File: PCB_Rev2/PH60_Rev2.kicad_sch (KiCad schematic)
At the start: 20 parts, among them J2 Conn_01x04, J3 Conn_01x02, Q1 AO3407, Q2 AO3407, U1 E73-2G4M08S1C, U2 AP2112K-3.3, U3 TP4054, U4 ProMicro, X1 32768kHz

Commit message: Rename
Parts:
- removed D63: 1N5819, Diode_SMD:D_SOD-323F, symbol nrfmicro-rescue:MBR0520
- removed D64: BLUE, LED_SMD:LED_0603_1608Metric, symbol Device:LED
- removed D65: RED, LED_SMD:LED_0603_1608Metric, symbol Device:LED
- removed J2: Conn_01x04, Connector_FFC-FPC:Molex_200528-0040_1x04-1MP_P1.00mm_Horizontal, symbol Connector_Generic:Conn_01x04
- removed J3: Conn_01x02, Connector_Molex:Molex_PicoBlade_53261-0271_1x02-1MP_P1.25mm_Horizontal, symbol Connector_Generic:Conn_01x02
- removed JP1: SolderJumper_2_Open, nrfmicro:Jumper_SMD, symbol Jumper:SolderJumper_2_Open
- removed Q1, Q2: AO3407, Package_TO_SOT_SMD:SOT-23, symbol nrfmicro-rescue:BSS83P
- removed R1: 100K, Resistor_SMD:R_0603_1608Metric, symbol nrfmicro-rescue:R
- removed R4, R8: 1K, Resistor_SMD:R_0603_1608Metric, symbol nrfmicro-rescue:R
- removed R5: RPROG, Resistor_SMD:R_0603_1608Metric, symbol nrfmicro-rescue:R
- removed R6: 820K, Resistor_SMD:R_0603_1608Metric, symbol Device:R
- removed R7, R9: 2M, Resistor_SMD:R_0603_1608Metric, symbol Device:R
- removed U1: E73-2G4M08S1C, nrfmicro:E73-2G4M08S1C-52840, symbol nrfmicro:E73-2G4M08S1C-52840
- removed U2: AP2112K-3.3, Package_TO_SOT_SMD:SOT-23-5, symbol Regulator_Linear:AP2112K-3.3
- removed U3: TP4054, Package_TO_SOT_SMD:SOT-23-5, symbol Battery_Management:MCP73832-2-OT
- removed U4: ProMicro, nrfmicro:pro_micro, symbol nrfmicro-rescue:ProMicro
- removed X1: 32768kHz, Crystal:Crystal_SMD_3215-2Pin_3.2x1.5mm, symbol Device:Crystal_Small
- added C1, C4: 10u, Capacitor_SMD:C_0402_1005Metric, symbol Device:C
- added C10, C8: 1u, Capacitor_SMD:C_0402_1005Metric, symbol Device:C
- added C11, C12, C13, C14, C15, C16, C5, C6, C7, C9: 100n, Capacitor_SMD:C_0402_1005Metric, symbol Device:C
- added C2, C3: 15p, Capacitor_SMD:C_0402_1005Metric, symbol Device:C
- added J2: Conn_01x02, Connector_PinHeader_1.00mm:PinHeader_1x02_P1.00mm_Vertical, symbol Connector_Generic:Conn_01x02
- added J3: Conn_01x04, Connector_FFC-FPC:Molex_200528-0040_1x04-1MP_P1.00mm_Horizontal, symbol Connector_Generic:Conn_01x04
- added R1, R5: 1k, Resistor_SMD:R_0402_1005Metric, symbol Device:R
- added R2: DNF, Resistor_SMD:R_0402_1005Metric, symbol Device:R
- added R3, R4: 27.4, Resistor_SMD:R_0402_1005Metric, symbol Device:R
- added U1: NCP1117-3.3_SOT223, Package_TO_SOT_SMD:SOT-223-3_TabPin2, symbol Regulator_Linear:NCP1117-3.3_SOT223
- added U2: W25Q128JVS, Package_SO:SOIC-8_5.23x5.23mm_P1.27mm, symbol Memory_Flash:W25Q128JVS
- added U3: RP2040, Package_DFN_QFN:QFN-56-1EP_7x7mm_P0.4mm_EP3.2x3.2mm, symbol MCU_RaspberryPi:RP2040
- added Y1: Crystal_GND24, Crystal:Crystal_SMD_3225-4Pin_3.2x2.5mm, symbol Device:Crystal_GND24
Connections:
- net GND: now also C1.2, C10.2, C2.2, C3.2, C4.2, C5.2, C6.2, C7.2, C8.2, J2.2 (Pin_2), J3.4 (Pin_4), U1.1 (GND), U2.4 (GND), U3.19 (TESTEN), U3.57 (GND), Y1.2, Y1.4
- net SWD: now also U3.25 (SWD)
- net VBUS: now also C1.1, J3.1 (Pin_1), U1.3 (VI)
- net col_0: now also U3.2 (GPIO0)
- net col_1: now also U3.3 (GPIO1)
- net col_10: now also U3.13 (GPIO10)
- net col_11: now also U3.14 (GPIO11)
- net col_12: now also U3.15 (GPIO12)
- net col_13: now also U3.16 (GPIO13)
- net col_2: now also U3.4 (GPIO2)
- net col_3: now also U3.5 (GPIO3)
- net col_4: now also U3.6 (GPIO4)
- net col_5: now also U3.7 (GPIO5)
- net col_6: now also U3.8 (GPIO6)
- net col_7: now also U3.9 (GPIO7)
- net col_8: now also U3.11 (GPIO8)
- net col_9: now also U3.12 (GPIO9)
- net row_0: now also U3.17 (GPIO14)
- net row_1: now also U3.18 (GPIO15)
- net row_2: now also U3.27 (GPIO16)
- net row_3: now also U3.28 (GPIO17)
- net row_4: now also U3.29 (GPIO18)
- new net: C11.2, C12.2, C13.2, C14.2, C15.2, C16.2, C9.2
- new net: R4.2, U3.46 (USB_DM)
- new net: C3.1, R5.1, Y1.1
- new net: R3.2, U3.47 (USB_DP)
- new net +1V1: C6.1, C7.1, C8.1, U3.23 (DVDD), U3.45 (VREG_VOUT), U3.50 (DVDD)
- new net +3V3: C10.1, C11.1, C12.1, C13.1, C14.1, C15.1, C16.1, C4.1, C5.1, C9.1, R2.1, U1.2 (VO), U2.8 (VCC), U3.1 (IOVDD), U3.10 (IOVDD), U3.22 (IOVDD), U3.33 (IOVDD), U3.42 (IOVDD), U3.43 (ADC_AVDD), U3.44 (VREG_IN), U3.48 (USB_VDD), U3.49 (IOVDD)
- new net QSPI_SCLK: U2.6 (CLK), U3.52 (QSPI_SCLK)
- new net QSPI_SD0: U2.5 (DI(IO0)), U3.53 (QSPI_SD0)
- new net QSPI_SD1: U2.2 (DO(IO1)), U3.55 (QSPI_SD1)
- new net QSPI_SD2: U2.3 (IO2), U3.54 (QSPI_SD2)
- new net QSPI_SD3: U2.7 (IO3), U3.51 (QSPI_SD3)
- new net QSPI_SS: R1.2, R2.2, U2.1 (~{CS})
- new net RUN: U3.26 (RUN)
- new net SWCLK: U3.24 (SWCLK)
- new net USB_D+: J3.3 (Pin_3), R3.1
- new net USB_D-: J3.2 (Pin_2), R4.1
- new net XIN: C2.1, U3.20 (XIN), Y1.3
- new net XOUT: R5.2, U3.21 (XOUT)
- new net ~{USB_BOOT}: J2.1 (Pin_1), R1.1
- no-connect marks 4 -> 13
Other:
- note removed: "1.4.x"
- note removed: "Battery monitor"
- note removed: "E73-2G4M08S1C pins: P0.02 P0.03 P0.04 P0.05 P0.06 P0.07 P0.08 P0.09 P0.10 P0.12 P0.13 P0.15 P0.17 P0.18 P0.20 P0.22 P0.24 P0.26 P0.28 P0.29 P0.30 P0.31 P1.00 P1.02 P1.04 P1.06 P1.09 P1.10 P1.11 P1.13"
- note removed: "Feather pins: P1.15 LED1 x P1.10 LED2 P0.15 BTN1 P0.19 BTN2 x P0.16 NEOPIXEL x P0.08 RX P0.06 TX P1.02 DFU P0.18 RESET"
- note removed: "Jan 3, 2021"
- note removed: "LiPo Charging"
- note removed: "Power and Filtering"
- note removed: "RProg = 1000/iBat iBat in amps RProg iBAT 10k 100mA 5k 200mA 2.5k 400mA 2k 500mA 1.25k 800mA"
- note removed: "nrfmicro"

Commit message: Routing
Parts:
- U1: footprint Package_TO_SOT_SMD:SOT-223-3_TabPin2 -> Package_TO_SOT_SMD:SOT-223
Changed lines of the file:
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@@
 			)
 		)
-		(property "Footprint" "Package_TO_SOT_SMD:SOT-223-3_TabPin2"
+		(property "Footprint" "Package_TO_SOT_SMD:SOT-223"
 			(at 129.54 213.36 0)
 			(effects

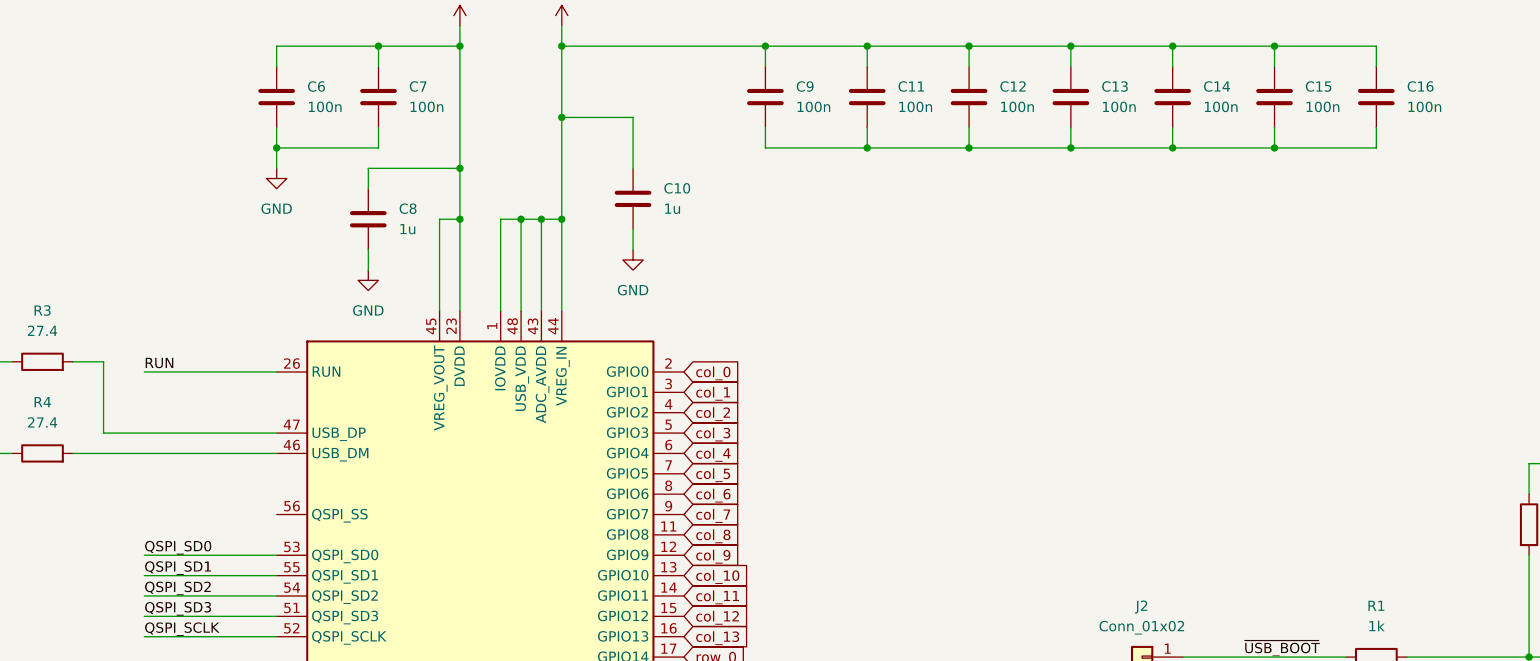
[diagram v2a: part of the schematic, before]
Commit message: PCB Update
Finished the wiring of PCB
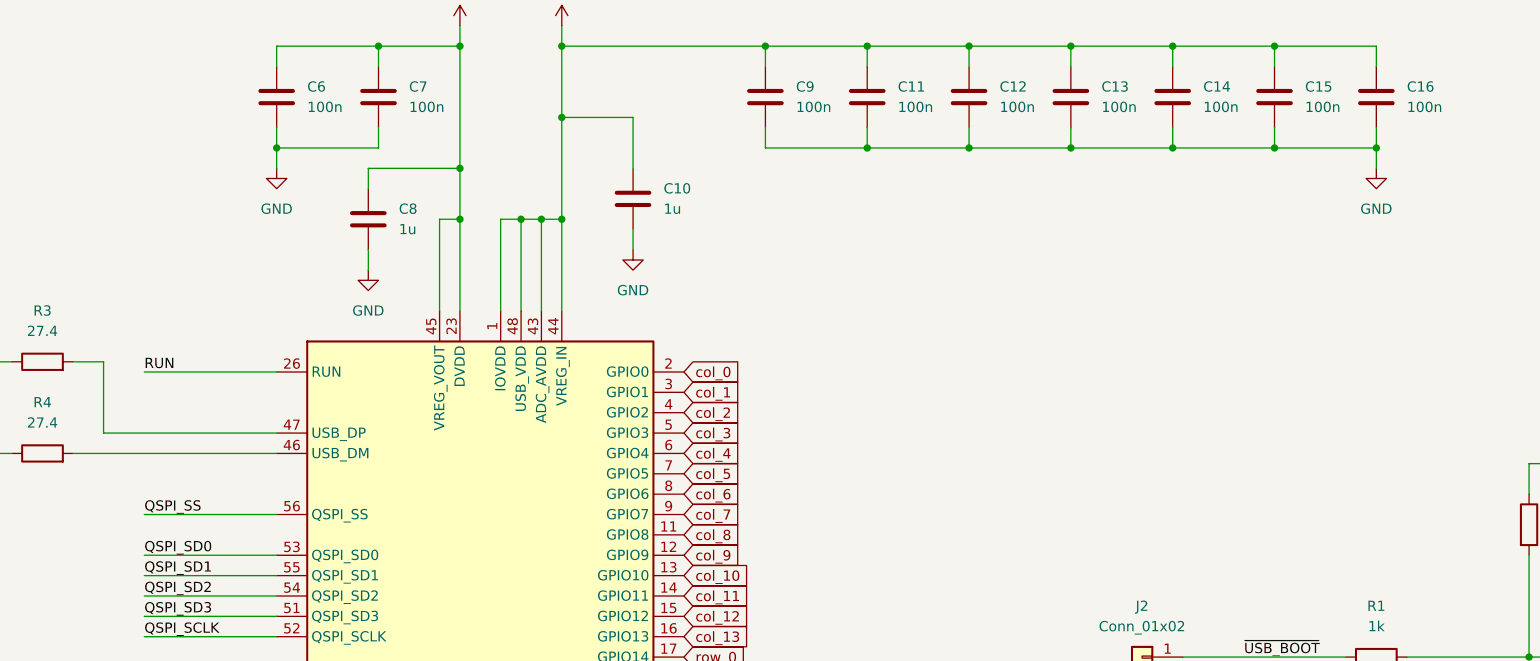
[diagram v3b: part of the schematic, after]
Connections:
- net GND: now also C11.2, C12.2, C13.2, C14.2, C15.2, C16.2, C9.2
- net QSPI_SS: now also U3.56 (QSPI_SS)
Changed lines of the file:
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@@
+	)
+	(junction
+		(at 220.98 45.72)
+		(diameter 0)
+		(color 0 0 0 0)
 	)
 	(junction
@@
 	(wire
 		(pts
+			(xy 67.31 91.44) (xy 83.82 91.44)
+		)
+		(stroke
+			(width 0)
+			(type default)
+		)
+	)
+	(wire
+		(pts
 			(xy 209.55 167.64) (xy 209.55 182.88)
 		)
@@
 		(pts
 			(xy 144.78 33.02) (xy 157.48 33.02)
+		)
+		(stroke
+			(width 0)
+			(type default)
+		)
+	)
+	(wire
+		(pts
+			(xy 220.98 45.72) (xy 220.98 48.26)
 		)
 		(stroke
@@
 	(label "RUN"
 		(at 67.31 73.66 0)
+		(fields_autoplaced yes)
+		(effects
+			(font
+				(size 1.27 1.27)
+			)
+			(justify left bottom)
+		)
+	)
+	(label "QSPI_SS"
+		(at 67.31 91.44 0)
 		(fields_autoplaced yes)
 		(effects
@@
 					(unit 1)
 				)
+			)
+		)
+	)
+	(symbol
+		(lib_id "power:GND")
+		(at 220.98 48.26 0)
+		(unit 1)
+		(exclude_from_sim no)
+		(in_bom yes)
+		(on_board yes)
+		(dnp no)
+		(fields_autoplaced yes)
+		(property "Reference" "#PWR021"
+			(at 220.98 54.61 0)
+			(effects
+				(font
+					(size 1.27 1.27)
+				)
+				(hide yes)
+			)
+		)
+		(property "Value" "GND"
+			(at 220.98 53.34 0)
+			(effects
+				(font
+					(size 1.27 1.27)
+				)
+			)
+		)
+		(property "Footprint" ""
+			(at 220.98 48.26 0)
+			(effects
+				(font
+					(size 1.27 1.27)
+				)
+				(hide yes)
+			)
+		)
+		(property "Datasheet" ""
+			(at 220.98 48.26 0)
+			(effects
+				(font
+					(size 1.27 1.27)
+				)
+				(hide yes)
+			)
+		)
+		(property "Description" "Power symbol creates a global label with name \"GND\" , ground"
+			(at 220.98 48.26 0)
+			(effects
+				(font
+					(size 1.27 1.27)
+				)
+				(hide yes)
+			)
+		)
+		(pin "1"
+		)
+		(instances
+			(project ""
+				(path "/dca0f898-8fdb-4522-a51d-f4f4238906e7"
+					(reference "#PWR021")
+					(unit 1)
+				)
